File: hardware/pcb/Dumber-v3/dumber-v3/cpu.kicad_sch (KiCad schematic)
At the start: 2 parts, among them U1 XBee_SMT, U2 STM32L031C6Tx

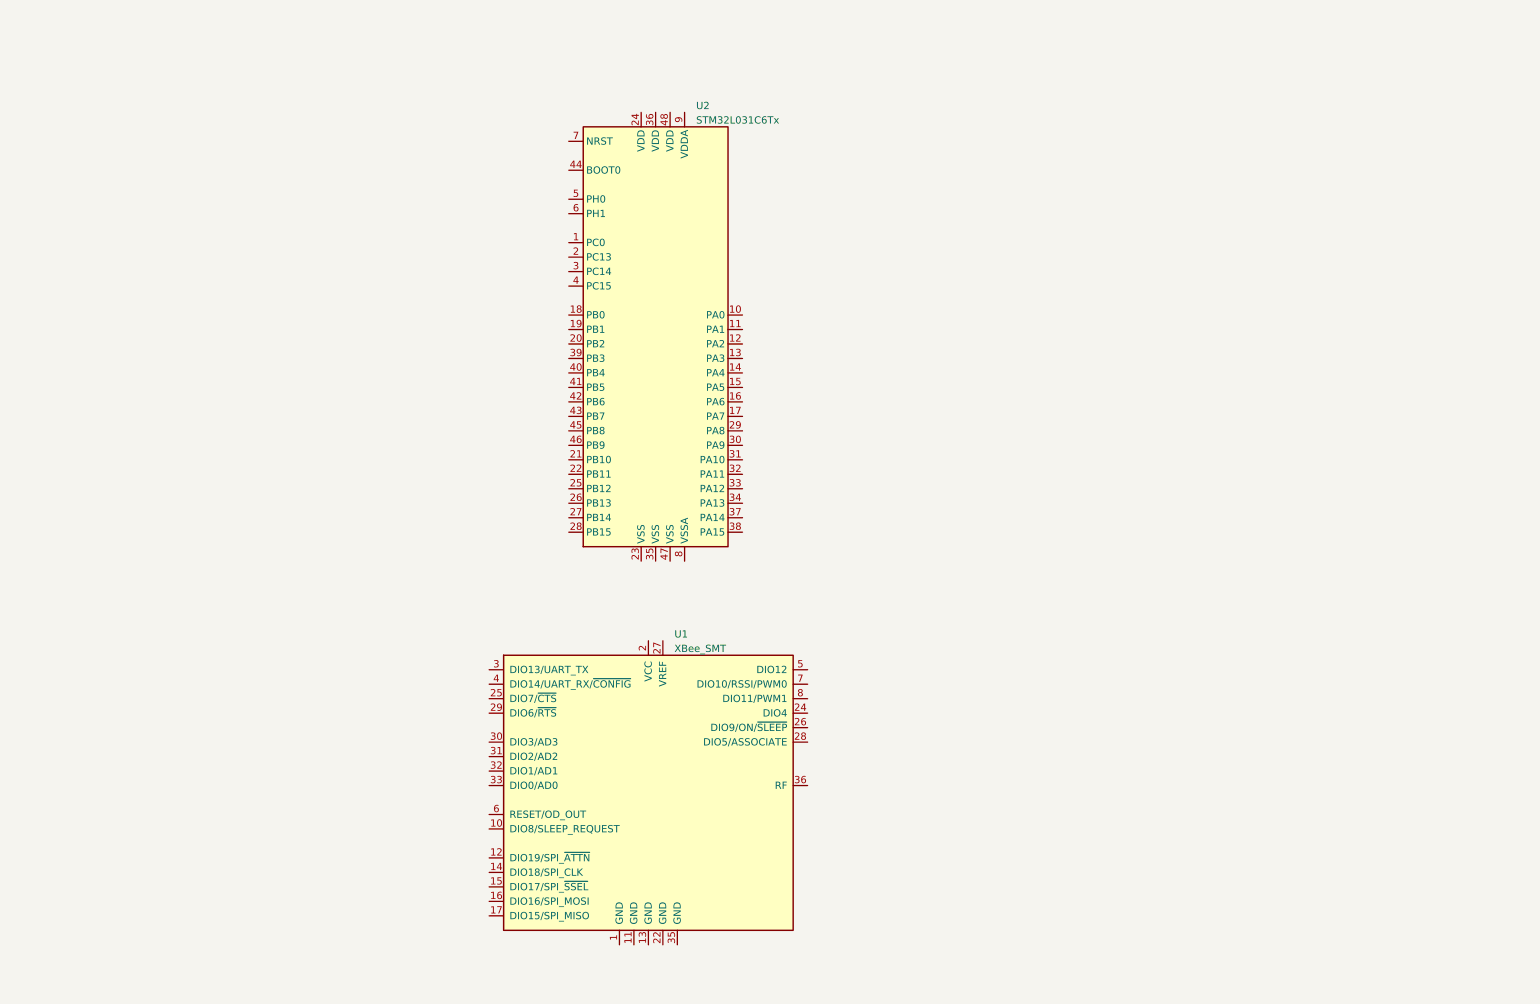
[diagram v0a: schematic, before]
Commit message: Schema complet, projet logiciel demarré
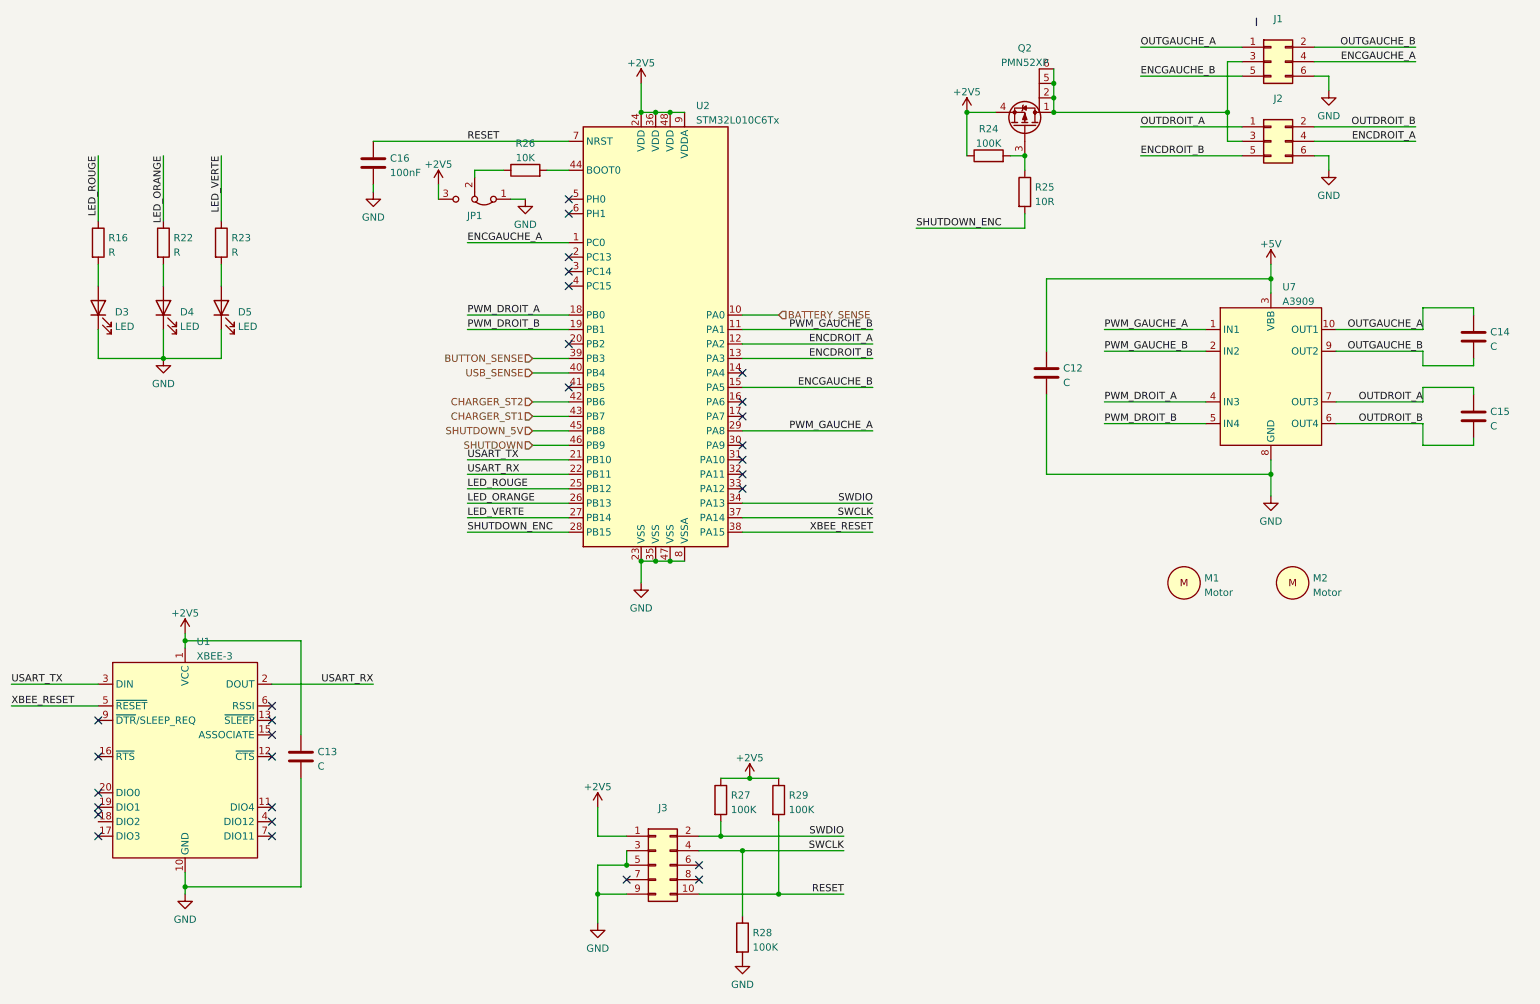
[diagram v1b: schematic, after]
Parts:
- removed U1: XBee_SMT, RF_Module:Digi_XBee_SMT, symbol RF_ZigBee:XBee_SMT
- added C12, C13, C14, C15: C, Capacitor_SMD:C_0805_2012Metric, symbol Device:C
- added C16: 100nF, Capacitor_SMD:C_0805_2012Metric, symbol Device:C
- added D3, D4, D5: LED, Diode_SMD:D_0805_2012Metric, symbol Device:LED
- added J1, J2: Conn_02x03_Odd_Even, Connector_IDC:IDC-Header_2x03_P2.54mm_Vertical, symbol Connector_Generic:Conn_02x03_Odd_Even
- added J3: Conn_02x05_Odd_Even, Connector_PinHeader_1.27mm:PinHeader_2x05_P1.27mm_Vertical_SMD, symbol Connector_Generic:Conn_02x05_Odd_Even
- added JP1: Jumper_3_Bridged12, Jumper:SolderJumper-3_P1.3mm_Open_RoundedPad1.0x1.5mm_NumberLabels, symbol Jumper:Jumper_3_Bridged12
- added M1, M2: Motor, INSA:Motor Pololu HPCB with encoder, symbol Insa:Motor
- added Q2: PMN52XP, Package_SO:TSOP-6_1.65x3.05mm_P0.95mm, symbol Insa:PMN52XP
- added R16, R22, R23: R, Resistor_SMD:R_0805_2012Metric, symbol Device:R
- added R24, R27, R28, R29: 100K, Resistor_SMD:R_0805_2012Metric, symbol Device:R
- added R25: 10R, Resistor_SMD:R_0805_2012Metric, symbol Device:R
- added R26: 10K, Resistor_SMD:R_0805_2012Metric, symbol Device:R
- added U1: XBEE-3, INSA:XBEE-3-TH, symbol Insa:XBEE-3
- added U7: A3909, Package_SO:SSOP-10_3.9x4.9mm_P1.00mm, symbol Insa:A3909
- U2: value STM32L031C6Tx -> STM32L010C6Tx
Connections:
- net ENCGAUCHE_A: now reaches U2.1 (PC0)
- net ENCGAUCHE_A: now also J1.4 (Pin_4)
- net BATTERY_SENSE: now reaches U2.10 (PA0)
- net PWM_GAUCHE_B: now reaches U2.11 (PA1)
- net PWM_GAUCHE_B: now also U7.2 (IN2)
- net ENCDROIT_A: now reaches U2.12 (PA2)
- net ENCDROIT_A: now also J2.4 (Pin_4)
- net ENCDROIT_B: now reaches U2.13 (PA3)
- net ENCDROIT_B: now also J2.5 (Pin_5)
- net ENCGAUCHE_B: now reaches U2.15 (PA5)
- net ENCGAUCHE_B: now also J1.5 (Pin_5)
- net PWM_DROIT_A: now reaches U2.18 (PB0)
- net PWM_DROIT_A: now also U7.4 (IN3)
- net PWM_DROIT_B: now reaches U2.19 (PB1)
- net PWM_DROIT_B: now also U7.5 (IN4)
- net USART_TX: now reaches U2.21 (PB10)
- net USART_TX: now also U1.3 (DIN)
- net USART_RX: now reaches U2.22 (PB11)
- net USART_RX: now also U1.2 (DOUT)
- net GND: now reaches U2.23 (VSS)
- net GND: now also U2.35 (VSS), U2.47 (VSS), U2.8 (VSSA), C12.2, C13.2, C16.2, D3.1 (K), D4.1 (K), D5.1 (K), J1.6 (Pin_6), J2.6 (Pin_6), J3.3 (Pin_3), J3.5 (Pin_5), J3.9 (Pin_9), JP1.1 (A), R28.2, U1.10 (GND), U7.8 (GND)
- net +2V5: now reaches U2.24 (VDD)
- net +2V5: now also U2.36 (VDD), U2.48 (VDD), U2.9 (VDDA), C13.1, J3.1 (Pin_1), JP1.3 (B), Q2.4 (S), R24.1, R27.1, R29.1, U1.1 (VCC)
- net LED_ROUGE: now reaches U2.25 (PB12)
- net LED_ROUGE: now also R16.1
- net LED_ORANGE: now reaches U2.26 (PB13)
- net LED_ORANGE: now also R22.1
- net LED_VERTE: now reaches U2.27 (PB14)
- net LED_VERTE: now also R23.1
- net SHUTDOWN_ENC: now reaches U2.28 (PB15)
- net SHUTDOWN_ENC: now also R25.2
- net PWM_GAUCHE_A: now reaches U2.29 (PA8)
- net PWM_GAUCHE_A: now also U7.1 (IN1)
- net SWDIO: now reaches U2.34 (PA13)
- net SWDIO: now also J3.2 (Pin_2), R27.2
- net SWCLK: now reaches U2.37 (PA14)
- net SWCLK: now also J3.4 (Pin_4), R28.1
- net XBEE_RESET: now reaches U2.38 (PA15)
- net XBEE_RESET: now also U1.5 (~{RESET})
- net BUTTON_SENSE: now reaches U2.39 (PB3)
- net USB_SENSE: now reaches U2.40 (PB4)
- net CHARGER_ST2: now reaches U2.42 (PB6)
- net CHARGER_ST1: now reaches U2.43 (PB7)
- net at U2.44 (BOOT0): now also R26.2
- net SHUTDOWN_5V: now reaches U2.45 (PB8)
- net SHUTDOWN: now reaches U2.46 (PB9)
- net RESET: now reaches U2.7 (NRST)
- net RESET: now also C16.1, J3.10 (Pin_10), R29.2
- new net: D4.2 (A), R22.2
- new net: D3.2 (A), R16.2
- new net: JP1.2 (C), R26.1
- new net: D5.2 (A), R23.2
- new net: J1.3 (Pin_3), J2.3 (Pin_3), Q2.1 (D), Q2.2 (D), Q2.5 (D), Q2.6 (D)
- new net: Q2.3 (G), R24.2, R25.1
- new net +5V: C12.1, U7.3 (VBB)
- new net OUTDROIT_A: C15.1, J2.1 (Pin_1), U7.7 (OUT3)
- new net OUTDROIT_B: C15.2, J2.2 (Pin_2), U7.6 (OUT4)
- new net OUTGAUCHE_A: C14.1, J1.1 (Pin_1), U7.10 (OUT1)
- new net OUTGAUCHE_B: C14.2, J1.2 (Pin_2), U7.9 (OUT2)
- no-connect marks 0 -> 30
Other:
- title: CPU -> CPU + Com + Motors

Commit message: PCB fini
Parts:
- added C17, C18, C19, C20: 100nF, Capacitor_SMD:C_0805_2012Metric, symbol Device:C
- C12, C13: value C -> 1µF
- C14, C15: value C -> 470nF
- R16, R22, R23: value R -> 1.5K
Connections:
- net +2V5: now also C17.1, C18.1, C19.1, C20.1
- net GND: now also C17.2, C18.2, C19.2, C20.2

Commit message: premiers modules du firwmare dumber 3
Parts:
- removed JP1: Jumper_3_Bridged12, Jumper:SolderJumper-3_P1.3mm_Open_RoundedPad1.0x1.5mm_NumberLabels, symbol Jumper:Jumper_3_Bridged12
- R16, R22: value 1.5K -> 1K
- R23: value 1.5K -> 820
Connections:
- net GND: now also R26.1
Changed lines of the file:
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@@
-    (stroke (width 0) (type default) (color 0 0 0 0))
-  )
-  (wire (pts (xy 93.98 50.8) (xy 93.98 53.34))
     (stroke (width 0) (type default) (color 0 0 0 0))
   )
@@
     (stroke (width 0) (type default) (color 0 0 0 0))
   )
-  (wire (pts (xy 106.68 53.34) (xy 109.22 53.34))
-    (stroke (width 0) (type default) (color 0 0 0 0))
-  )
   (wire (pts (xy 266.7 82.55) (xy 275.59 82.55))
     (stroke (width 0) (type default) (color 0 0 0 0))
@@
     (effects (font (size 1.27 1.27)) (justify right bottom))
   )
-  (label "RESET" (at 99.06 43.18 0)
+  (label "RESET" (at 105.41 43.18 0)
     (effects (font (size 1.27 1.27)) (justify left bottom))
   )
@@
     (effects (font (size 1.27 1.27)) (justify right))
   )
-  (symbol (lib_id "power:GND") (at 109.22 53.34 0) (unit 1)
-    (in_bom yes) (on_board yes) (fields_autoplaced)
-    (property "Reference" "#PWR030" (id 0) (at 109.22 59.69 0)
-      (effects (font (size 1.27 1.27)) hide)
-    )
-    (property "Value" "GND" (id 1) (at 109.22 57.7834 0))
-    (property "Footprint" "" (id 2) (at 109.22 53.34 0)
-      (effects (font (size 1.27 1.27)) hide)
-    )
-    (property "Datasheet" "" (id 3) (at 109.22 53.34 0)
+  (symbol (lib_id "power:GND") (at 100.33 49.53 0) (unit 1)
+    (in_bom yes) (on_board yes) (fields_autoplaced)
+    (property "Reference" "#PWR030" (id 0) (at 100.33 55.88 0)
+      (effects (font (size 1.27 1.27)) hide)
+    )
+    (property "Value" "GND" (id 1) (at 100.33 53.9734 0))
+    (property "Footprint" "" (id 2) (at 100.33 49.53 0)
+      (effects (font (size 1.27 1.27)) hide)
+    )
+    (property "Datasheet" "" (id 3) (at 100.33 49.53 0)
       (effects (font (size 1.27 1.27)) hide)
     )
@@
     (pin "2")
   )
-  (symbol (lib_id "Jumper:Jumper_3_Bridged12") (at 100.33 53.34 180) (unit 1)
-    (in_bom yes) (on_board yes) (fields_autoplaced)
-    (property "Reference" "JP1" (id 0) (at 100.33 56.2346 0))
-    (property "Value" "Jumper_3_Bridged12" (id 1) (at 100.33 58.7715 0)
-      (effects (font (size 1.27 1.27)) hide)
-    )
-    (property "Footprint" "Jumper:SolderJumper-3_P1.3mm_Open_RoundedPad1.0x1.5mm_NumberLabels" (id 2) (at 100.33 53.34 0)
-      (effects (font (size 1.27 1.27)) hide)
-    )
-    (property "Datasheet" "~" (id 3) (at 100.33 53.34 0)
-      (effects (font (size 1.27 1.27)) hide)
-    )
-    (pin "1")
-    (pin "2")
-    (pin "3")
-  )
   (symbol (lib_id "power:GND") (at 250.19 48.26 0) (unit 1)
     (in_bom yes) (on_board yes) (fields_autoplaced)
@@
       (effects (font (size 1.27 1.27)) (justify left))
     )
-    (property "Value" "1.5K" (id 1) (at 36.068 62.6622 0)
+    (property "Value" "1K" (id 1) (at 36.068 62.6622 0)
       (effects (font (size 1.27 1.27)) (justify left))
     )
@@
       (effects (font (size 1.27 1.27)) (justify left))
     )
-    (property "Value" "1.5K" (id 1) (at 47.498 62.6622 0)
+    (property "Value" "1K" (id 1) (at 47.498 62.6622 0)
       (effects (font (size 1.27 1.27)) (justify left))
     )
@@
   )
   (symbol (lib_id "Device:R") (at 109.22 48.26 90) (unit 1)
-    (in_bom yes) (on_board yes) (fields_autoplaced)
-    (property "Reference" "R26" (id 0) (at 109.22 43.5442 90))
-    (property "Value" "10K" (id 1) (at 109.22 46.0811 90))
+    (in_bom yes) (on_board yes)
+    (property "Reference" "R26" (id 0) (at 106.68 45.72 90))
+    (property "Value" "10K" (id 1) (at 111.76 45.72 90))
     (property "Footprint" "Resistor_SMD:R_0805_2012Metric" (id 2) (at 109.22 50.038 90)
       (effects (font (size 1.27 1.27)) hide)
@@
       (effects (font (size 1.27 1.27)) (justify left))
     )
-    (property "Value" "1.5K" (id 1) (at 57.658 62.6622 0)
+    (property "Value" "820" (id 1) (at 57.658 62.6622 0)
       (effects (font (size 1.27 1.27)) (justify left))
     )
@@
   )
   (symbol (lib_id "Insa:XBEE-3") (at 49.53 171.45 0) (unit 1)
-    (in_bom yes) (on_board yes) (fields_autoplaced)
+    (in_bom yes) (on_board yes)
     (property "Reference" "U1" (id 0) (at 51.5494 130.971 0)
       (effects (font (size 1.27 1.27)) (justify left))
@@
     (pin "9")
   )
-  (symbol (lib_id "power:+2V5") (at 93.98 50.8 0) (unit 1)
-    (in_bom yes) (on_board yes) (fields_autoplaced)
-    (property "Reference" "#PWR029" (id 0) (at 93.98 54.61 0)
-      (effects (font (size 1.27 1.27)) hide)
-    )
-    (property "Value" "+2V5" (id 1) (at 93.98 47.2242 0))
-    (property "Footprint" "" (id 2) (at 93.98 50.8 0)
-      (effects (font (size 1.27 1.27)) hide)
-    )
-    (property "Datasheet" "" (id 3) (at 93.98 50.8 0)
-      (effects (font (size 1.27 1.27)) hide)
-    )
-    (pin "1")
-  )
   (symbol (lib_id "Connector_Generic:Conn_02x03_Odd_Even") (at 240.03 29.21 0) (unit 1)

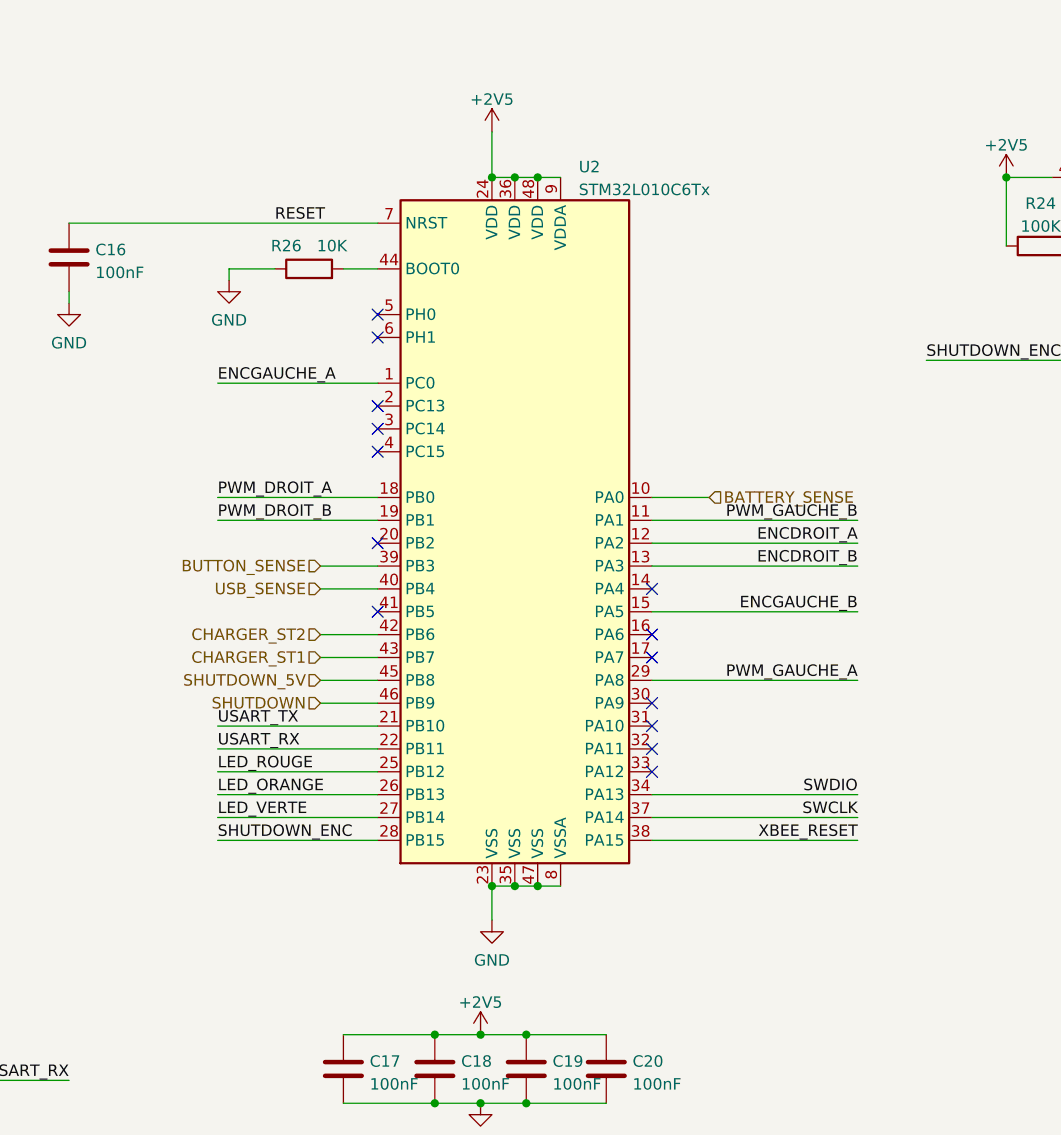
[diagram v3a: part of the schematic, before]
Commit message: Modification du PCB suite au passage au MCU STM32L071CBT6
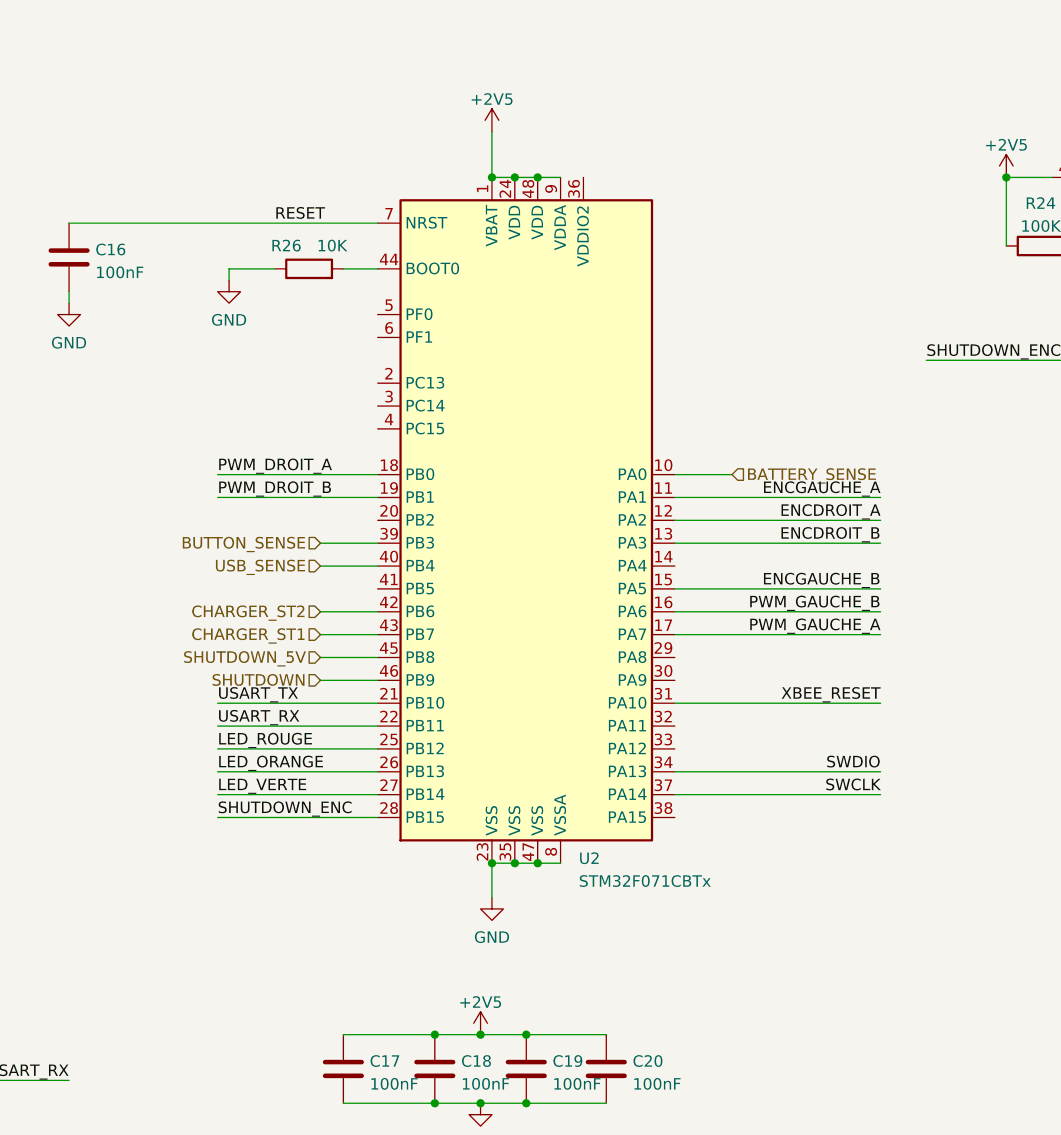
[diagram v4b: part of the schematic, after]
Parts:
- removed U2: STM32L010C6Tx, Package_QFP:LQFP-48_7x7mm_P0.5mm, symbol MCU_ST_STM32L0:STM32L031C6Tx
- added U2: STM32F071CBTx, Package_QFP:LQFP-48_7x7mm_P0.5mm, symbol MCU_ST_STM32F0:STM32F071CBTx
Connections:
- net +2V5: now also U2.1 (VBAT), U2.24 (VDD), U2.48 (VDD), U2.9 (VDDA)
- net BATTERY_SENSE: now also U2.10 (PA0)
- net BUTTON_SENSE: now also U2.39 (PB3)
- net CHARGER_ST1: now also U2.43 (PB7)
- net CHARGER_ST2: now also U2.42 (PB6)
- net ENCDROIT_A: now also U2.12 (PA2)
- net ENCDROIT_B: now also U2.13 (PA3)
- net ENCGAUCHE_A: now also U2.11 (PA1)
- net ENCGAUCHE_B: now also U2.15 (PA5)
- net GND: now also U2.23 (VSS), U2.35 (VSS), U2.47 (VSS), U2.8 (VSSA)
- net LED_ORANGE: now also U2.26 (PB13)
- net LED_ROUGE: now also U2.25 (PB12)
- net LED_VERTE: now also U2.27 (PB14)
- net PWM_DROIT_A: now also U2.18 (PB0)
- net PWM_DROIT_B: now also U2.19 (PB1)
- net PWM_GAUCHE_A: now also U2.17 (PA7)
- net PWM_GAUCHE_B: now also U2.16 (PA6)
- net RESET: now also U2.7 (NRST)
- net SHUTDOWN: now also U2.46 (PB9)
- net SHUTDOWN_5V: now also U2.45 (PB8)
- net SHUTDOWN_ENC: now also U2.28 (PB15)
- net SWCLK: now also U2.37 (PA14)
- net SWDIO: now also U2.34 (PA13)
- net USART_RX: now also U2.22 (PB11)
- net USART_TX: now also U2.21 (PB10)
- net USB_SENSE: now also U2.40 (PB4)
- net XBEE_RESET: now also U2.31 (PA10)
- net at R26.2: now also U2.44 (BOOT0)
- no-connect marks 30 -> 16
